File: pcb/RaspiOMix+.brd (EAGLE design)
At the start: 65 x 56 mm, 81 parts, among them IC1 MCP3424-E/SL, IC2 DS1307, IC4 MCP3424-E/SL, K1 PIN20X2, U1 EEPROM24

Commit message: Routage
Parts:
- removed C11, C12, C13, C14, C2, C3, C4, C5: 100nf, rcl:C0805
- removed IC1, IC4: MCP3424-E/SL, eagleParts:SOIC-14
- removed R10, R11, R12, R13, R21, R23, R25, R27: 6.8k 1%, rcl:M0805
- removed R20, R22, R24, R26, R6, R7, R8, R9: 10k 0.1%, rcl:M0805
- added C16, C17, CA0, CA1, CA2, CA3, CA4, CA5, CA6, CA7: 100nf, rcl:C0805
- added CON_IO_4, CON_IO_5, CON_IO_6, CON_IO_7: (no value), Seeedstudio_Connector:4P-2.0-W/O-BUCKLE
- added RA0, RA1, RA2, RA3, RA4, RA5, RA6, RA7: 10k 0.1%, rcl:M0805
- added RB0, RB1, RB2, RB3, RB4, RB5, RB6, RB7: 6.8k 1%, rcl:M0805
- added U$1, U$3: MCP3424-E/ST, eagleParts:SOP65P640X120-14N
- moved U2 52.1 mm to (23.5, 64.1)
- moved J_ADR2 51.7 mm to (77.5, 77.2), flipped to the bottom
- moved J_ADR0 38.7 mm to (23.2, 24.7), flipped to the bottom
- moved J_ADR1 37.9 mm to (24.0, 22.9), flipped to the bottom
- moved CON_AN_4 23.4 mm to (51.8, 21.6)
- moved CON_AN_7 23.4 mm to (51.8, 2.54)
- moved J_ADR3 16.8 mm to (54.3, 28.6), flipped to the bottom, turned to 180 degrees
- moved IC3 15.2 mm to (20.1, 17.5)
- moved CON_AN_5 15.1 mm to (51.8, 15.2)
- moved CON_AN_6 15.1 mm to (51.8, 8.89)
- moved CON_AN_0 14.0 mm to (38.1, 21.6)
- moved CON_AN_1 14.0 mm to (38.1, 15.2)
- moved CON_AN_2 14.0 mm to (38.1, 8.89)
- moved CON_AN_3 14.0 mm to (38.1, 2.54)
- moved R5 7.24 mm to (50.2, 66.0)
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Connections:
- new net IO4: CON_IO_3.2, CON_IO_4.1
- new net IO5: CON_IO_4.2, CON_IO_5.1
- new net IO6: CON_IO_5.2, CON_IO_6.1
- new net IO7: CON_IO_6.2, CON_IO_7.1
- new net N$13: U2.2
- new net N$14: U2.3
- new net N$15: U2.4
- new net N$16: U2.5
- new net N$17: U2.13
- new net N$18: U2.12
- new net N$19: U2.11
- new net N$20: U2.10
- net +3V3: now also C17.1, U$1.6, U$3.6, U2.1, U2.8; no longer IC1.6, IC4.6
- net +5V: now also C16.1, CON_IO_4.3, CON_IO_5.3, CON_IO_6.3, CON_IO_7.3, U2.14
- net ADR0: now also U$1.9, U$3.9; no longer IC1.9, IC4.9
- net ADR1: now also U$1.10, U$3.10; no longer IC1.10, IC4.10
- net AN0: now also RA0.2; no longer R20.2
- net AN1: now also RA1.2; no longer R22.2
- net AN2: now also RA2.2; no longer R24.2
- net AN3: now also RA3.2; no longer R26.2
- net AN4: now also RA4.2; no longer R9.2
- net AN5: now also RA5.2; no longer R8.2
- net AN6: now also RA6.2; no longer R7.2
- net AN7: now also RA7.2; no longer R6.2
- net IO0: now also CON_IO_7.2; no longer CON_IO_3.2
- net N$10: now also CA5.1, RA5.1, RB5.2, U$3.3; no longer C12.1, IC4.3, R12.2, R8.1
- net N$11: now also CA4.1, RA4.1, RB4.2, U$3.1; no longer C11.1, IC4.1, R13.2, R9.1
- net N$4: now also CA3.1, RA3.1, RB3.2, U$1.13; no longer C5.1, IC1.13, R26.1, R27.2
- net N$5: now also CA2.1, RA2.1, RB2.2, U$1.11; no longer C4.1, IC1.11, R24.1, R25.2
- net N$6: now also CA1.1, RA1.1, RB1.2, U$1.3; no longer C3.1, IC1.3, R22.1, R23.2
- net N$7: now also CA0.1, RA0.1, RB0.2, U$1.1; no longer C2.1, IC1.1, R20.1, R21.2
- net N$8: now also CA7.1, RA7.1, RB7.2, U$3.13; no longer C14.1, IC4.13, R10.2, R6.1
- net N$9: now also CA6.1, RA6.1, RB6.2, U$3.11; no longer C13.1, IC4.11, R11.2, R7.1
- net PI_SCL: now also U$1.8, U$3.8; no longer IC1.8, IC4.8
- net PI_SDA: now also U$1.7, U$3.7; no longer IC1.7, IC4.7
- net VSS: now also C16.2, C17.2, CA0.2, CA1.2, CA2.2, CA3.2, CA4.2, CA5.2, CA6.2, CA7.2, CON_IO_4.4, CON_IO_5.4, CON_IO_6.4, CON_IO_7.4, RB0.1, RB1.1, RB2.1, RB3.1, RB4.1, RB5.1, RB6.1, RB7.1, U$1.12, U$1.14, U$1.2, U$1.4, U$1.5, U$3.12, U$3.14, U$3.2, U$3.4, U$3.5, U2.7; no longer C11.2, C12.2, C13.2, C14.2, C2.2, C3.2, C4.2, C5.2, IC1.12, IC1.14, IC1.2, IC1.4, IC1.5, IC4.12, IC4.14, IC4.2, IC4.4, IC4.5, R10.1, R11.1, R12.1, R13.1, R21.1, R23.1, R25.1, R27.1
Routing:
- added copper zone on layer 16, net VSS
- removed copper zone on layer 16, net GND

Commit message: Routage PCB
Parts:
- removed CR1220: (no value), adafruit:CR1220-THM
- removed IO6: TPPAD1-13, testpad:P1-13
- removed U$3: MCP3424-E/ST, eagleParts:SOP65P640X120-14N
- added ICA1: MCP3424-E/ST, eagleParts:SOP65P640X120-14N
- added IO??: TPPAD1-13, testpad:P1-13
- JP1: device jumper:JP1 -> FLYFISH:PIN_W_2
- moved CON_IO_7 59.0 mm to (21.6, 14.0)
- moved C6 56.9 mm to (39.8, 32.1), turned to 180 degrees
- moved C28 54.2 mm to (44.1, 34.0)
- moved J_ADR2 53.3 mm to (54.9, 28.9), turned to 180 degrees
- moved TP1 51.2 mm to (8.05, 59.0)
- moved CON_IO_6 50.1 mm to (21.6, 20.3)
- moved C16 43.2 mm to (28.3, 31.1), turned to 270 degrees
- moved CON_IO_5 42.5 mm to (21.6, 26.7)
- moved CON_IO_4 38.2 mm to (21.6, 33.0)
- moved Q6 37.3 mm to (56.3, 48.6), turned to 180 degrees
- moved C17 35.5 mm to (31.1, 39.1), turned to 180 degrees
- moved IC2 33.9 mm to (50.0, 46.2), turned to 180 degrees
- moved C15 32.4 mm to (55.6, 33.7)
- moved C10 31.5 mm to (60.0, 33.7), turned to 180 degrees
- moved C7 30.6 mm to (46.7, 42.5), turned to 270 degrees
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- renumbered U$1 to ICA0
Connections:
- net N$1 renamed ID_SC
- net N$2 renamed ID_SD
- removed net N$13: U2.2
- removed net N$14: U2.3
- removed net N$15: U2.4
- removed net N$16: U2.5
- removed net N$17: U2.13
- removed net N$18: U2.12
- removed net N$19: U2.11
- removed net N$20: U2.10
- new net ADR2: ICA1.9, J_ADR3.2
- new net ADR3: ICA1.10, J_ADR2.2
- new net PI_IO4: K1.35, U2.2
- new net PI_IO5: K1.33, U2.3
- new net PI_IO7: K1.29, U2.5
- new net PI_IO??: K1.22
- net +3V3: now also ICA1.6; no longer U$3.6
- net ADR0: no longer J_ADR3.2, U$3.9
- net ADR1: no longer J_ADR2.2, U$3.10
- net IO0: now also IC3.16; no longer IC3.20
- net IO1: now also IC3.17; no longer IC3.18
- net IO2: now also IC3.18; no longer IC3.17
- net IO3: now also IC3.20; no longer IC3.16
- net IO4: now also U2.13
- net IO5: now also U2.12
- net IO6: now also U2.11
- net IO7: now also U2.10
- net N$10: now also ICA1.1; no longer U$3.3
- net N$11: now also ICA1.3; no longer U$3.1
- net N$58: now also JP1.2; no longer CR1220.+1, JP1.1
- net N$8: now also ICA1.11; no longer U$3.13
- net N$9: now also ICA1.13; no longer U$3.11
- net PI_DIP0: now also R5.2, SW1.3; no longer R4.2, SW1.4
- net PI_DIP1: now also R4.2, SW1.4; no longer R5.2, SW1.3
- net PI_IO0: now also IC3.5; no longer IC3.1
- net PI_IO1: now also IC3.4; no longer IC3.3
- net PI_IO2: now also IC3.3; no longer IC3.4
- net PI_IO3: now also IC3.1; no longer IC3.5
- net PI_IO6: now also K1.31, U2.4; no longer IO6.TP, K1.22
- net PI_RX: now also IC3.6; no longer IC3.9
- net PI_SCL: now also IC3.8, ICA1.8; no longer IC3.7, U$3.8
- net PI_SDA: now also IC3.9, ICA1.7; no longer IC3.6, U$3.7
- net PI_TX: now also IC3.7; no longer IC3.8
- net RX: now also IC3.15; no longer IC3.12
- net SCL: now also IC3.13; no longer IC3.14
- net SDA: now also IC3.12; no longer IC3.15
- net TX: now also IC3.14; no longer IC3.13
- net VSS: now also ICA1.12, ICA1.14, ICA1.2, ICA1.4, ICA1.5, JP1.1; no longer CR1220.-, JP1.2, U$3.12, U$3.14, U$3.2, U$3.4, U$3.5
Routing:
- net +5V: track 0.00 -> 160.7 mm
- net PI_DIP0: track 0.00 -> 64.6 mm, vias 0 -> 1
- net SCL: track 0.00 -> 61.7 mm, vias 0 -> 2
- net IO0: track 0.00 -> 55.6 mm
- net PI_DIP1: track 0.00 -> 54.4 mm, vias 0 -> 1
- net SDA: track 0.00 -> 54.0 mm, vias 0 -> 2
- net +3V3: track 0.00 -> 51.7 mm
- net RX: track 0.00 -> 48.9 mm, vias 0 -> 1
- net TX: track 0.00 -> 46.7 mm, vias 0 -> 1
- net N$4: track 0.00 -> 43.0 mm, vias 0 -> 2
- net AN4: track 0.00 -> 42.5 mm, vias 0 -> 1
- net IO3: track 0.00 -> 41.1 mm
- net PI_SDA: track 0.00 -> 39.8 mm, vias 0 -> 2
- net N$8: track 0.00 -> 35.7 mm
- net IO2: track 0.00 -> 34.0 mm
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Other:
- board text added: "0"
- board text added: "1"
- board text added: "2"
- board text added: "3"
- board text added: "4"
- board text added: "5"
- board text added: "6"
- board text added: "7"

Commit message: RaspiO'Mix rev 1.0.0
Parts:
- removed C15: (no value), rcl:B/3528-21R
- removed C16, C17, C28, C30, C31: 100nf, rcl:C0805
- removed ICA0: MCP3424-E/ST, eagleParts:SOP65P640X120-14N
- removed IO??: TPPAD1-13, testpad:P1-13
- removed R14: 330, rcl:M0805
- removed R19: 1k, rcl:M0805
- removed U2: (no value), adafruit:TSSOP14
- added C11, C12, C2, C4, C5: 100nf, rcl:C0805
- added C3: 100nF, resistor:C0805K
- added IC1: (no value), adafruit:TSSOP20
- added IC4: MCP3424-E/ST, eagleParts:SOP65P640X120-14N
- added IC6: TMP101, tmp10x:SOT23-6
- added LOGO1: OSHW_LOGO_FILLX0350-NT, ohw-logo:OSHW_FILLX350_NOTEXT
- added R6, R7: 3k9, resistor:M0805
- added TP10, TP11, TP12, TP2, TP3, TP4, TP5, TP6, TP7, TP8, TP9: TPTP12R, testpad:TP12R
- C1: value 100nF -> 220uf; device resistor:C0805K -> rcl:PANASONIC_D
- C10: value 100nf -> (none); device rcl:C0805 -> rcl:B/3528-21R
- C6: value (none) -> 100nf; device rcl:B/3528-21R -> rcl:C0805
- C8: value 220uf -> (none); device rcl:PANASONIC_D -> rcl:B/3528-21R
- C9: value 220uf -> 100nf; device rcl:PANASONIC_D -> rcl:C0805
- IC2: value DS1307 -> (none); device eagleParts:SOIC-8 -> adafruit:TSSOP14
- IC3: value (none) -> DS1307; device adafruit:TSSOP20 -> eagleParts:SOIC-8
- R1: value 3k9 -> 330; device resistor:M0805 -> rcl:M0805
- R2: value 3k9 -> 10k; device resistor:M0805 -> rcl:M0805
- R3: value 1k -> 10k; device resistor:M0805 -> rcl:M0805
- R4: value 10k -> 1k
- R5: value 10k -> 1k; device rcl:M0805 -> resistor:M0805
- moved TP1 74.5 mm to (62.9, 8.57)
- moved C9 35.1 mm to (36.1, 31.8)
- moved R5 28.9 mm to (34.1, 42.9)
- moved R3 28.6 mm to (62.6, 47.5), turned to 270 degrees
- moved IC3 24.4 mm to (50.0, 46.2)
- moved C8 24.1 mm to (40.9, 32.3), turned to 180 degrees
- moved R2 23.1 mm to (60.1, 47.5), turned to 270 degrees
- moved C7 20.8 mm to (28.7, 32.1)
- moved IC2 20.0 mm to (33.0, 35.6), turned to 90 degrees
- moved C1 19.4 mm to (18.8, 41.9), turned to 90 degrees
- moved R4 12.6 mm to (48.3, 43.0), turned to 0 degrees
- moved R1 12.3 mm to (48.3, 37.8), turned to 180 degrees
- moved C6 9.37 mm to (33.5, 39.1)
- moved C10 2.54 mm to (57.5, 33.7), turned to 0 degrees
- moved POWER 2.27 mm to (44.6, 37.8)
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- renumbered ICA1 to IC5
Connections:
- removed net GND: C1.2
- removed net PI_CE0: K1.24
- removed net PI_CE1: K1.26
- removed net PI_IO??: K1.22
- removed net PI_MISO: K1.21
- removed net PI_MOSI: K1.19
- removed net PI_SCLK: K1.23
- new net N$1: K1.40, TP2.TP
- new net N$12: K1.36, TP4.TP
- new net N$13: K1.32, TP5.TP
- new net N$14: K1.37, TP6.TP
- new net N$15: K1.22, TP7.TP
- new net N$16: K1.24, TP8.TP
- new net N$17: K1.26, TP9.TP
- new net N$18: K1.19, TP10.TP
- new net N$19: K1.21, TP11.TP
- new net N$2: K1.38, TP3.TP
- new net N$20: K1.23, TP12.TP
- net +3V3: now also C10.+, C11.2, C12.1, C3.1, C4.1, C6.1, C8.+, C9.2, IC1.10, IC1.2, IC2.1, IC2.8, IC4.6, IC6.P$4, R4.2, R5.2, R6.2, R7.2; no longer C1.1, C10.2, C15.+, C17.1, C28.2, C30.1, C6.+, IC3.10, IC3.2, ICA0.6, R1.2, R19.2, R2.2, R3.2, U2.1, U2.8
- net +5V: now also C1.+, C2.1, C5.1, IC1.19, IC2.14, IC3.8; no longer C16.1, C31.1, C8.+, C9.+, IC2.8, IC3.19, U2.14
- net ADR0: now also IC4.9; no longer ICA0.9
- net ADR1: now also IC4.10; no longer ICA0.10
- net ID_SC: now also R6.1; no longer R1.1
- net ID_SD: now also R7.1; no longer R2.1
- net INTC: now also IC3.7, R4.1; no longer IC2.7, R19.1
- net IO0: now also IC1.16; no longer IC3.16
- net IO1: now also IC1.17; no longer IC3.17
- net IO2: now also IC1.18; no longer IC3.18
- net IO3: now also IC1.20; no longer IC3.20
- net IO4: now also IC2.13; no longer U2.13
- net IO5: now also IC2.12; no longer U2.12
- net IO6: now also IC2.11; no longer U2.11
- net IO7: now also IC2.10; no longer U2.10
- net N$3: now also R5.1; no longer R3.1
- net N$33: now also IC3.1; no longer IC2.1
- net N$34: now also IC3.2; no longer IC2.2
- net N$39: now also R1.2; no longer R14.2
- net N$4: now also IC4.13; no longer ICA0.13
- net N$5: now also IC4.11; no longer ICA0.11
- net N$58: now also IC3.3; no longer IC2.3
- net N$6: now also IC4.3; no longer ICA0.3
- net N$7: now also IC4.1; no longer ICA0.1
- net PI_DIP0: now also R2.2, SW1.4; no longer R5.2, SW1.3
- net PI_DIP1: now also R3.2, SW1.3; no longer R4.2, SW1.4
- net PI_IO0: now also IC1.5; no longer IC3.5
- net PI_IO1: now also IC1.4; no longer IC3.4
- net PI_IO2: now also IC1.3; no longer IC3.3
- net PI_IO3: now also IC1.1; no longer IC3.1
- net PI_IO4: now also IC2.2; no longer U2.2
- net PI_IO5: now also IC2.3; no longer U2.3
- net PI_IO6: now also IC2.4; no longer U2.4
- net PI_IO7: now also IC2.5; no longer U2.5
- net PI_RX: now also IC1.6; no longer IC3.6
- net PI_SCL: now also IC1.8, IC4.8, IC6.P$1; no longer IC3.8, ICA0.8
- net PI_SDA: now also IC1.9, IC4.7, IC6.P$6; no longer IC3.9, ICA0.7
- net PI_TX: now also IC1.7; no longer IC3.7
- net RX: now also IC1.15; no longer IC3.15
- net SCL: now also IC1.13, IC3.6; no longer IC2.6, IC3.13
- net SDA: now also IC1.12, IC3.5; no longer IC2.5, IC3.12
- net TX: now also IC1.14; no longer IC3.14
- net VSS: now also C1.-, C10.-, C11.1, C12.2, C2.2, C3.2, C4.2, C5.2, C6.2, C9.1, IC1.11, IC2.7, IC3.4, IC4.12, IC4.14, IC4.2, IC4.4, IC4.5, IC6.P$2, R1.1, R2.1, R3.1; no longer C10.1, C15.-, C16.2, C17.2, C28.1, C30.2, C31.2, C6.-, C9.-, IC2.4, IC3.11, ICA0.12, ICA0.14, ICA0.2, ICA0.4, ICA0.5, R14.1, R4.1, R5.1, U2.7
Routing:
- net +3V3: track 51.7 -> 194.4 mm, vias 0 -> 4
- net +5V: track 160.7 -> 285.8 mm, vias 0 -> 6
- net VSS: track 13.3 -> 63.3 mm, vias 2 -> 32
- net PI_SDA: track 39.8 -> 89.1 mm, vias 2 -> 3
- net SDA: track 54.0 -> 99.4 mm, vias 2 -> 4
- net SCL: track 61.7 -> 103.4 mm, vias 2 -> 4
- net PI_SCL: track 33.6 -> 69.4 mm, vias 2 -> 3
- net IO4: track 26.5 -> 41.1 mm, vias 1 -> 2
- net IO7: track 26.5 -> 37.7 mm
- net IO5: track 7.22 -> 18.3 mm, vias 0 -> 1
- net N$58: track 8.72 -> 19.2 mm
- net ADR2: track 0.00 -> 7.21 mm, vias 0 -> 1
- net PI_DIP1: track 54.4 -> 59.5 mm, vias 1 -> 2
- net AN4: track 42.5 -> 37.9 mm
- net ADR3: track 0.00 -> 3.09 mm, vias 0 -> 1
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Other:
- outline, holes or cut-outs redrawn
- board text added: "*"
- board text added: "* Push-pull only"
- board text added: "2014/11"
- board text added: "5V"
- board text added: "ADR0"
- board text added: "ADR1"
- board text added: "ADR2"
- board text added: "ADR3"
- board text added: "AN"
- board text added: "AN0"
- board text added: "AN1"
- board text added: "AN2"
- board text added: "AN3"
- board text added: "AN4"
- board text added: "AN5"
- board text added: "AN6"
- board text added: "AN7"
- board text added: "I2C"
- board text added: "IO0"
- board text added: "IO1"
- board text added: "IO2"
- board text added: "IO3"
- board text added: "IO4"
- board text added: "IO5"
- board text added: "IO6"
- board text added: "IO7"
- board text added: "RX"
- board text added: "RaspiO'Mix+"
- board text added: "SCL"
- board text added: "SDA"
- board text added: "Serial"
- board text added: "TX"
- board text added: "rev 1.0.0"
- board text added: "www.digitalspirit.org"
- board text added: "x3"

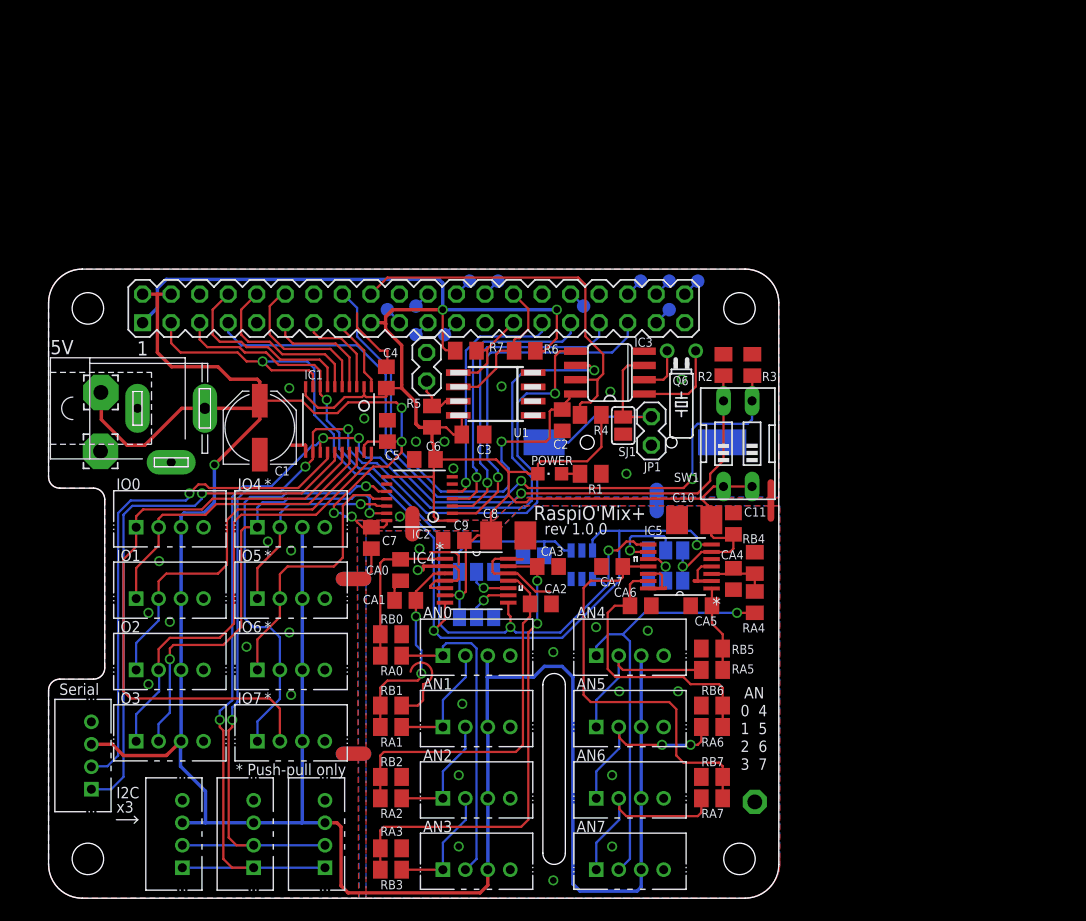
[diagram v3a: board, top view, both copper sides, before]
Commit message: RaspiO'Mix+
Modif
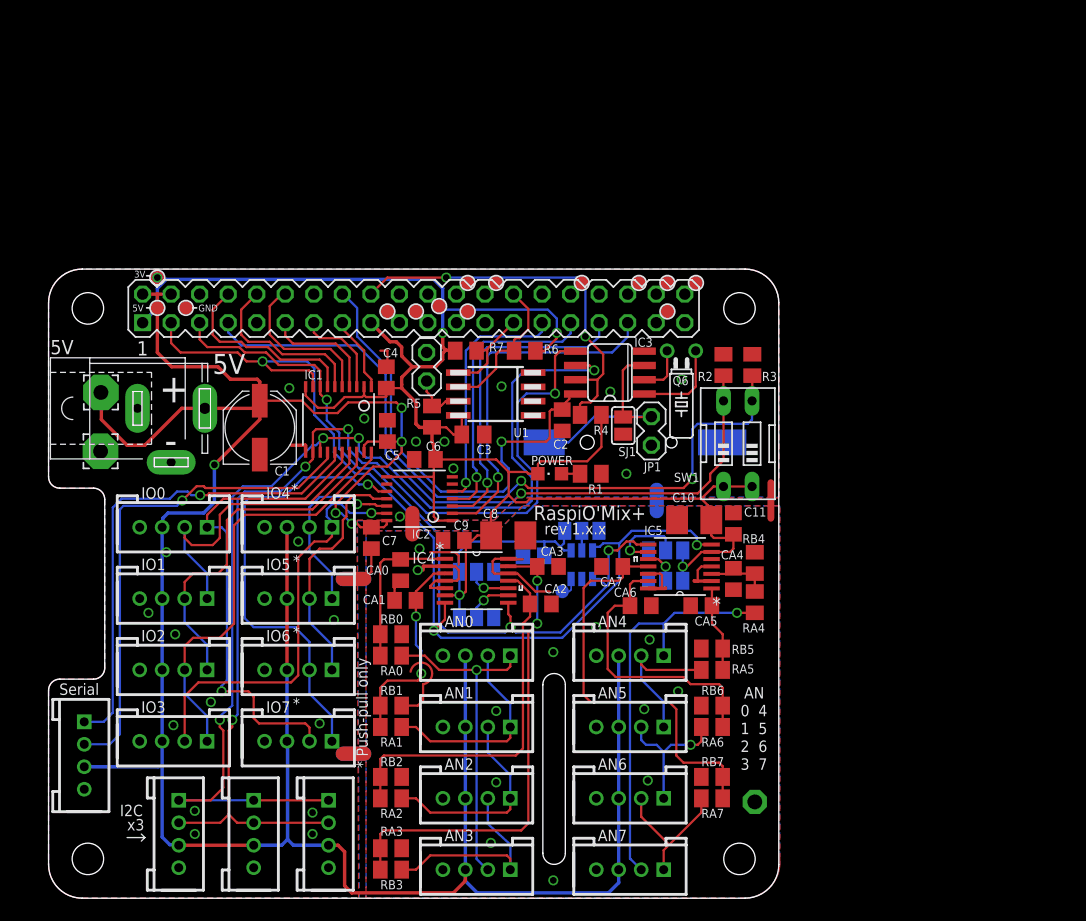
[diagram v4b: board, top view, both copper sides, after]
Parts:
- added J_ADR4: (no value), jumper:SJ_2
- added TALM, TP3V, TP5V, TPGND: TPTP12R, testpad:TP12R
- CON_AN_0, CON_AN_1, CON_AN_2, CON_AN_3, CON_AN_4, CON_AN_5, CON_AN_6, CON_AN_7, CON_I2C_0, CON_I2C_1, CON_I2C_2, CON_IO_0, CON_IO_1, CON_IO_2, CON_IO_3, CON_IO_4, CON_IO_5, CON_IO_6, CON_IO_7, CON_SERIAL: device Seeedstudio_Connector:4P-2.0-W/O-BUCKLE -> Seeedstudio_Connector:4P-2.0
- moved CON_I2C_0 6.67 mm to (11.6, 5.71), turned to 270 degrees
- moved CON_I2C_1 6.35 mm to (18.3, 5.71), turned to 270 degrees
- moved TP12 2.92 mm to (37.3, 52.2), flipped to the top
- moved TP5 2.07 mm to (47.5, 54.8), flipped to the top
- moved TP11 2.06 mm to (32.7, 52.2), flipped to the top
- moved TP7 2.06 mm to (34.8, 52.7), flipped to the top
- moved CON_IO_4 0.64 mm to (22.2, 33.0), turned to 180 degrees
- moved CON_IO_5 0.64 mm to (22.2, 26.7), turned to 180 degrees
- moved CON_IO_6 0.64 mm to (22.2, 20.3), turned to 180 degrees
- moved CON_IO_7 0.64 mm to (22.2, 14.0), turned to 180 degrees
- moved CON_SERIAL 0.64 mm to (3.17, 12.7), turned to 270 degrees
- moved CON_IO_0 0.32 mm to (11.1, 33.0), turned to 180 degrees
- moved CON_IO_1 0.32 mm to (11.1, 26.7), turned to 180 degrees
- moved CON_IO_2 0.32 mm to (11.1, 20.3), turned to 180 degrees
- moved CON_IO_3 0.32 mm to (11.1, 14.0), turned to 180 degrees
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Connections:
- new net N$21: IC6.P$5, J_ADR4.2
- new net N$22: IC6.P$3, TALM.TP
- net +3V3: now also J_ADR4.1, TP3V.TP
- net +5V: now also TP5V.TP
- net VSS: now also J_ADR4.3, TPGND.TP
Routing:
- net +5V: track 285.8 -> 266.9 mm
- net IO0: track 54.7 -> 43.7 mm, vias 0 -> 1
- net AN3: track 10.8 -> 18.5 mm
- net AN1: track 10.8 -> 18.5 mm
- net AN2: track 10.8 -> 18.5 mm
- net RX: track 48.5 -> 43.6 mm
- net AN6: track 17.1 -> 12.7 mm, vias 2 -> 1
- net SCL: track 103.4 -> 99.1 mm
- net AN7: track 17.1 -> 12.9 mm
- net VSS: track 63.3 -> 59.1 mm, vias 32 -> 34
- net IO4: track 41.1 -> 37.6 mm, vias 2 -> 1
- net SDA: track 99.4 -> 96.1 mm
- net IO7: track 37.7 -> 40.7 mm
- net IO6: track 24.6 -> 21.7 mm
- net IO2: track 34.1 -> 31.8 mm
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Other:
- board text added: "+"
- board text added: "-"
- board text added: "3V"
- board text added: "GND"
- board text added: "rev 1.x.x"
- board text removed: "rev 1.0.0"
